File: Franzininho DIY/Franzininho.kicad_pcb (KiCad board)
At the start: 2 copper layers, 51.1 x 30 mm, 30 parts, among them IC1 ATTINY85 - 20PU, J1 M03PTH, U1 L78L05_TO92, X1 USB-A-H

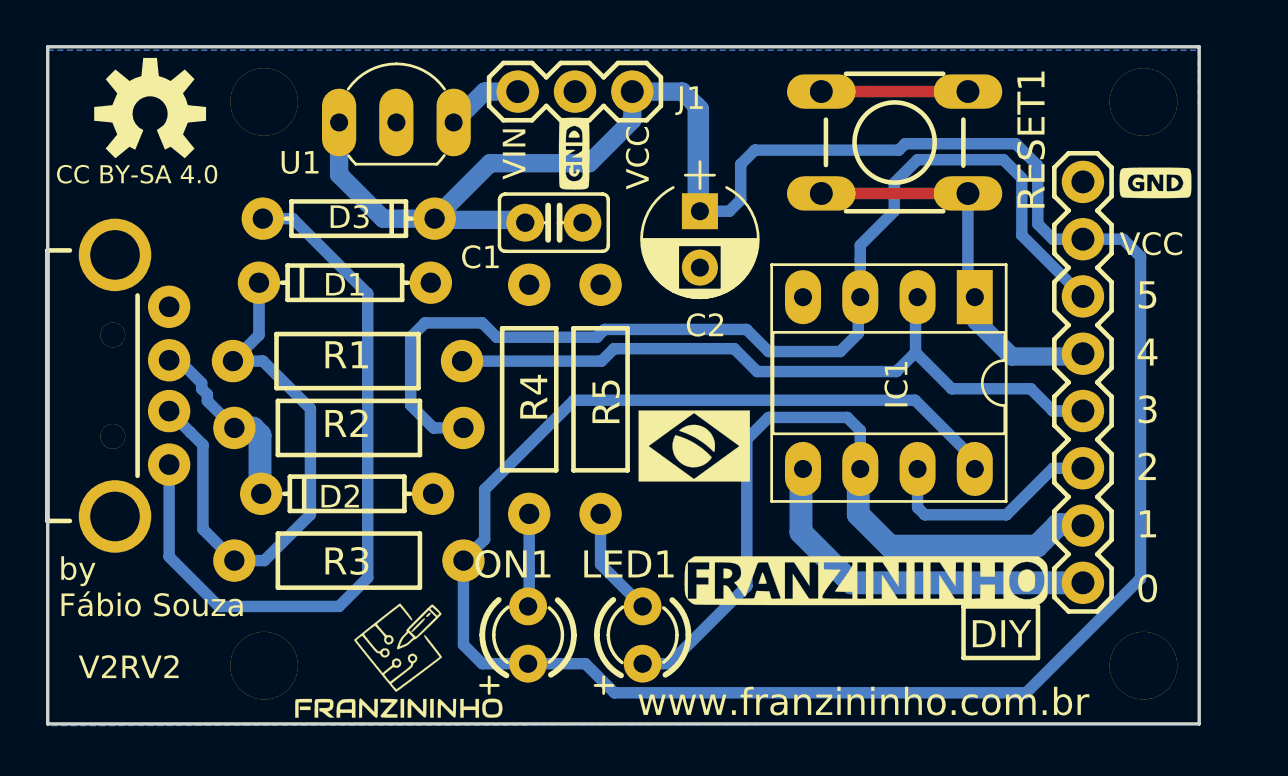
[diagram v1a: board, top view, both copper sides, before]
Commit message: Ajuste da área de cobre para de solid para thermal relief para facilitar a soldagem. Ajuste de silks. Adicionado um ponto para indicar o pino 1 do mcu. Refeito área de cobre com um clearece menor
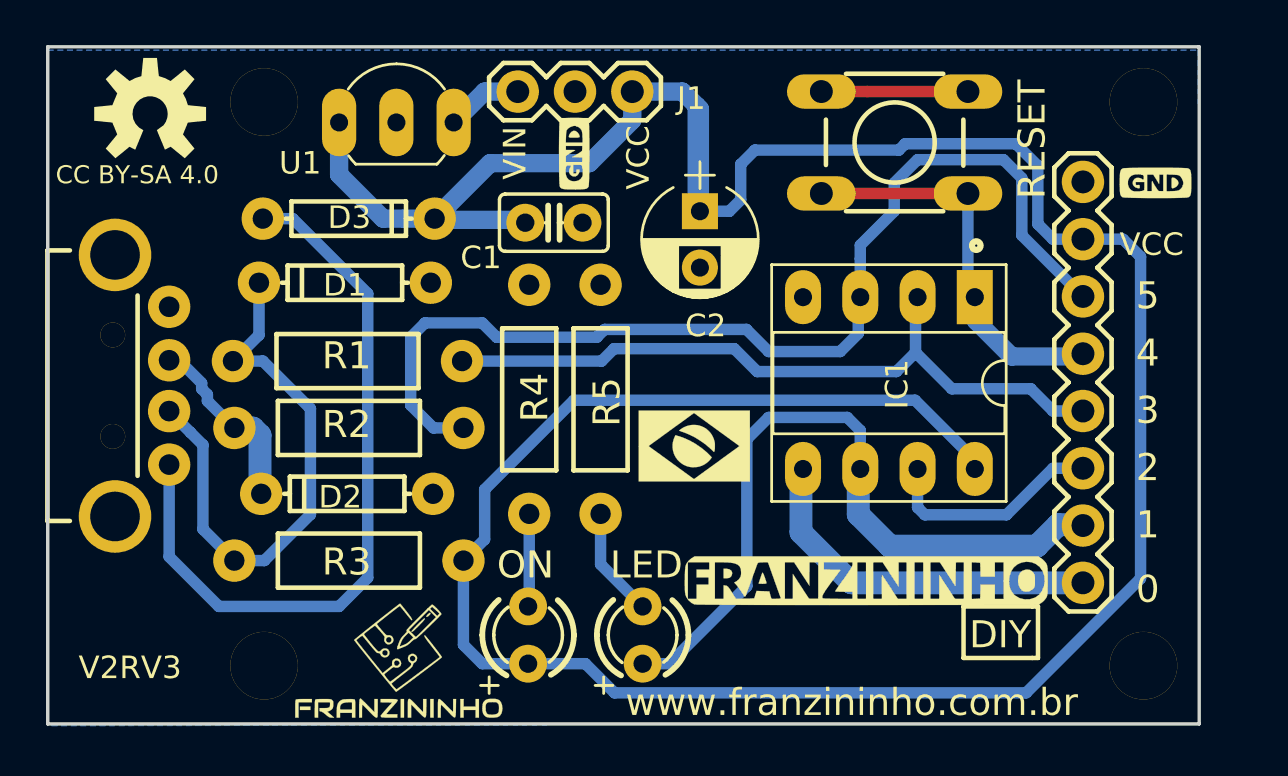
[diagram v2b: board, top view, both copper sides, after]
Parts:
- renumbered LED1 to LED, ON1 to ON, RESET1 to RESET
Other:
- board text added: "V2RV3"
- board text removed: "V2RV2"
- board text removed: "by Fábio Souza"
